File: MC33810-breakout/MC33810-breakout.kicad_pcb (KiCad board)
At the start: 2 copper layers, 78 x 50 mm, 38 parts, among them J1 6473423-1, P1 Pad, P2 Pad, P3 Pad, P4 Pad, Q1 ISL9V3040S3S, Q2 ISL9V3040S3S, Q3 ISL9V3040S3S, Q4 ISL9V3040S3S, U1 MCZ33810EK, U2 XC6206P332MR

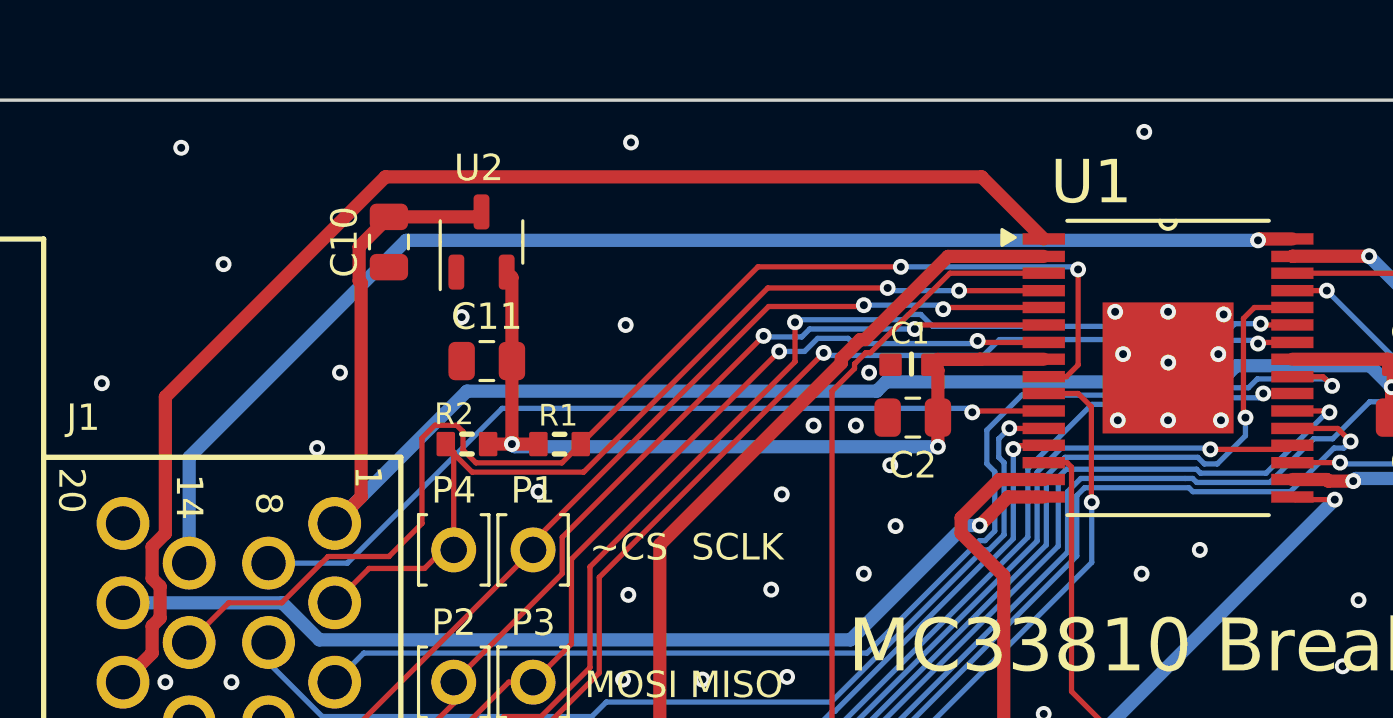
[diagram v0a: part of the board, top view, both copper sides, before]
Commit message: Fix LDO
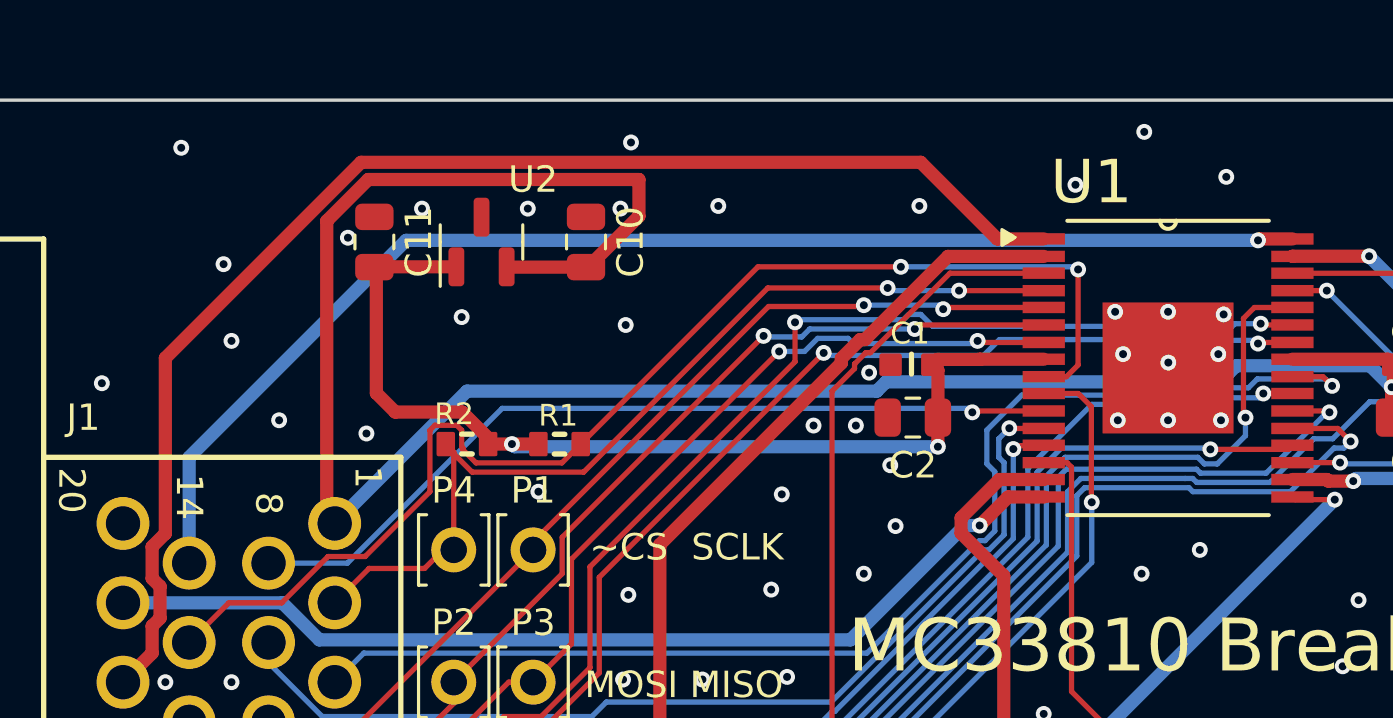
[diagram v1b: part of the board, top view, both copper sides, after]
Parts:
- U2: value XC6206P332MR -> XC6202P332MR-G; footprint Package_TO_SOT_SMD:SOT-23-3 -> Package_TO_SOT_SMD:SOT-23
- moved C10 7.45 mm to (98.0, 99.4), turned to -90 degrees
- moved C11 6.19 mm to (90.0, 99.4), turned to -90 degrees
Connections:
- U2 pad 1: GND -> +3.3V
- U2 pad 2: +3.3V -> +BATT
- U2 pad 3: +BATT -> GND
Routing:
- net +BATT: track 64.8 -> 79.9 mm
- net +3.3V: track 32.1 -> 38.5 mm
- net /OUT_INJ1: track 49.3 -> 50.6 mm
- net /~OUTEN: track 48.1 -> 47.6 mm
- net GND: vias 91 -> 100
